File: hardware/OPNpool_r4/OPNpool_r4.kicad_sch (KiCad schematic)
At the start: 15 parts, among them J2 RS485-TERM-SPTAF, U1 MAX3485CSA+

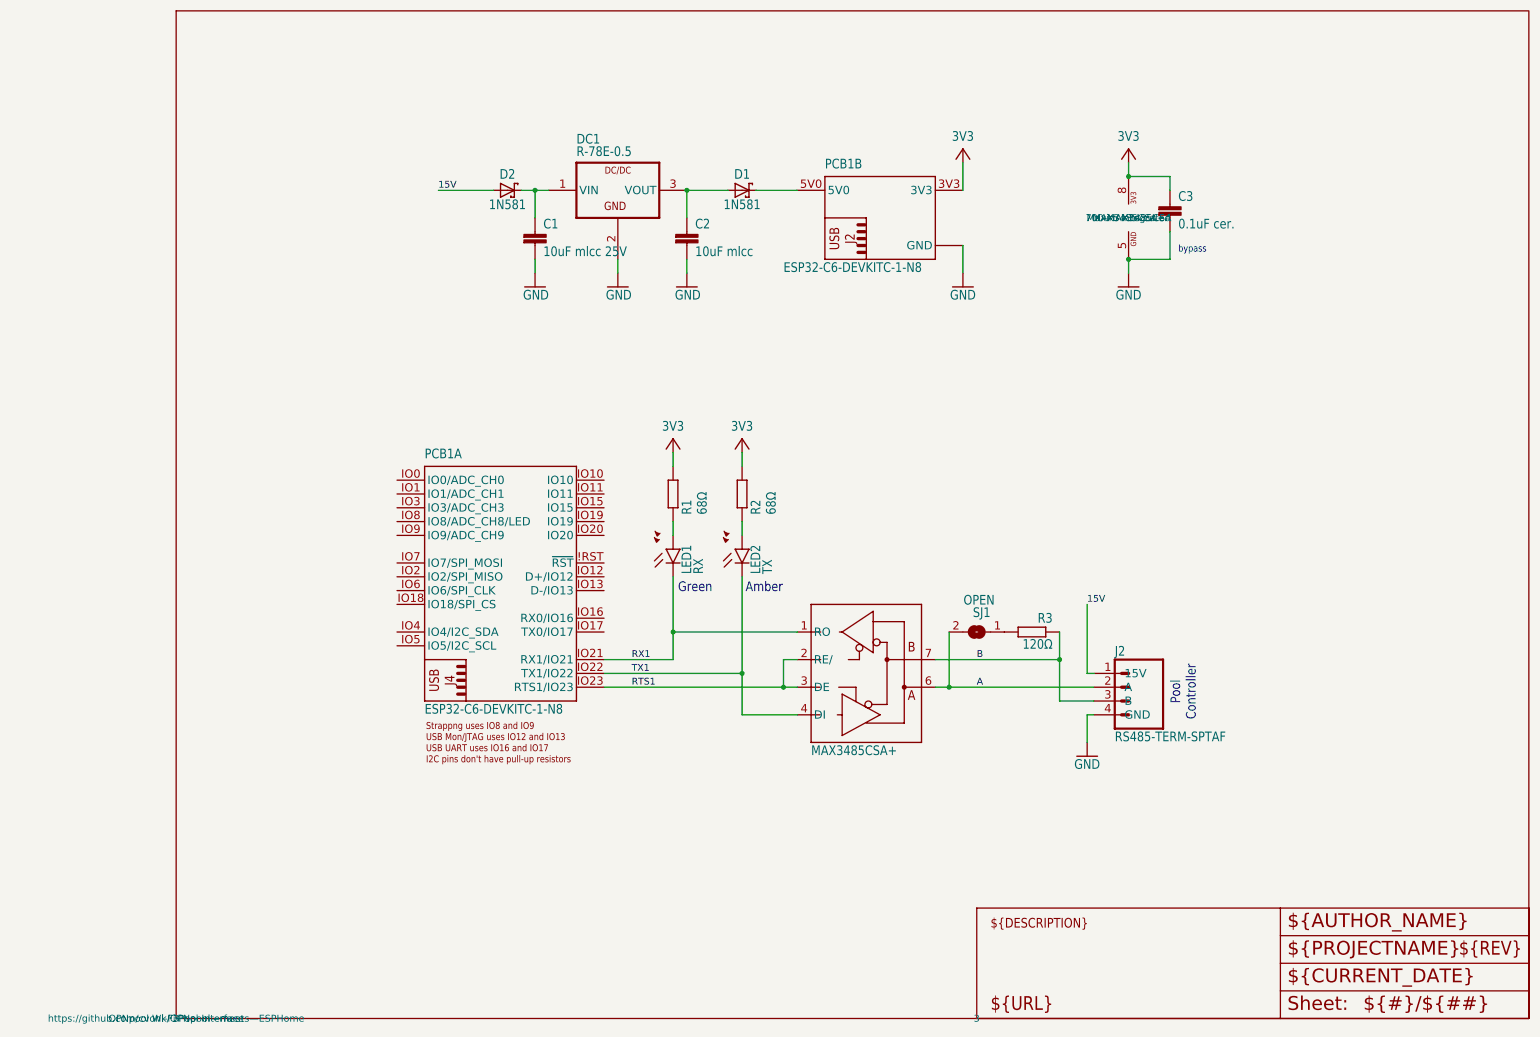
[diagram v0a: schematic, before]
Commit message: move from Eagle to KiCad symbols
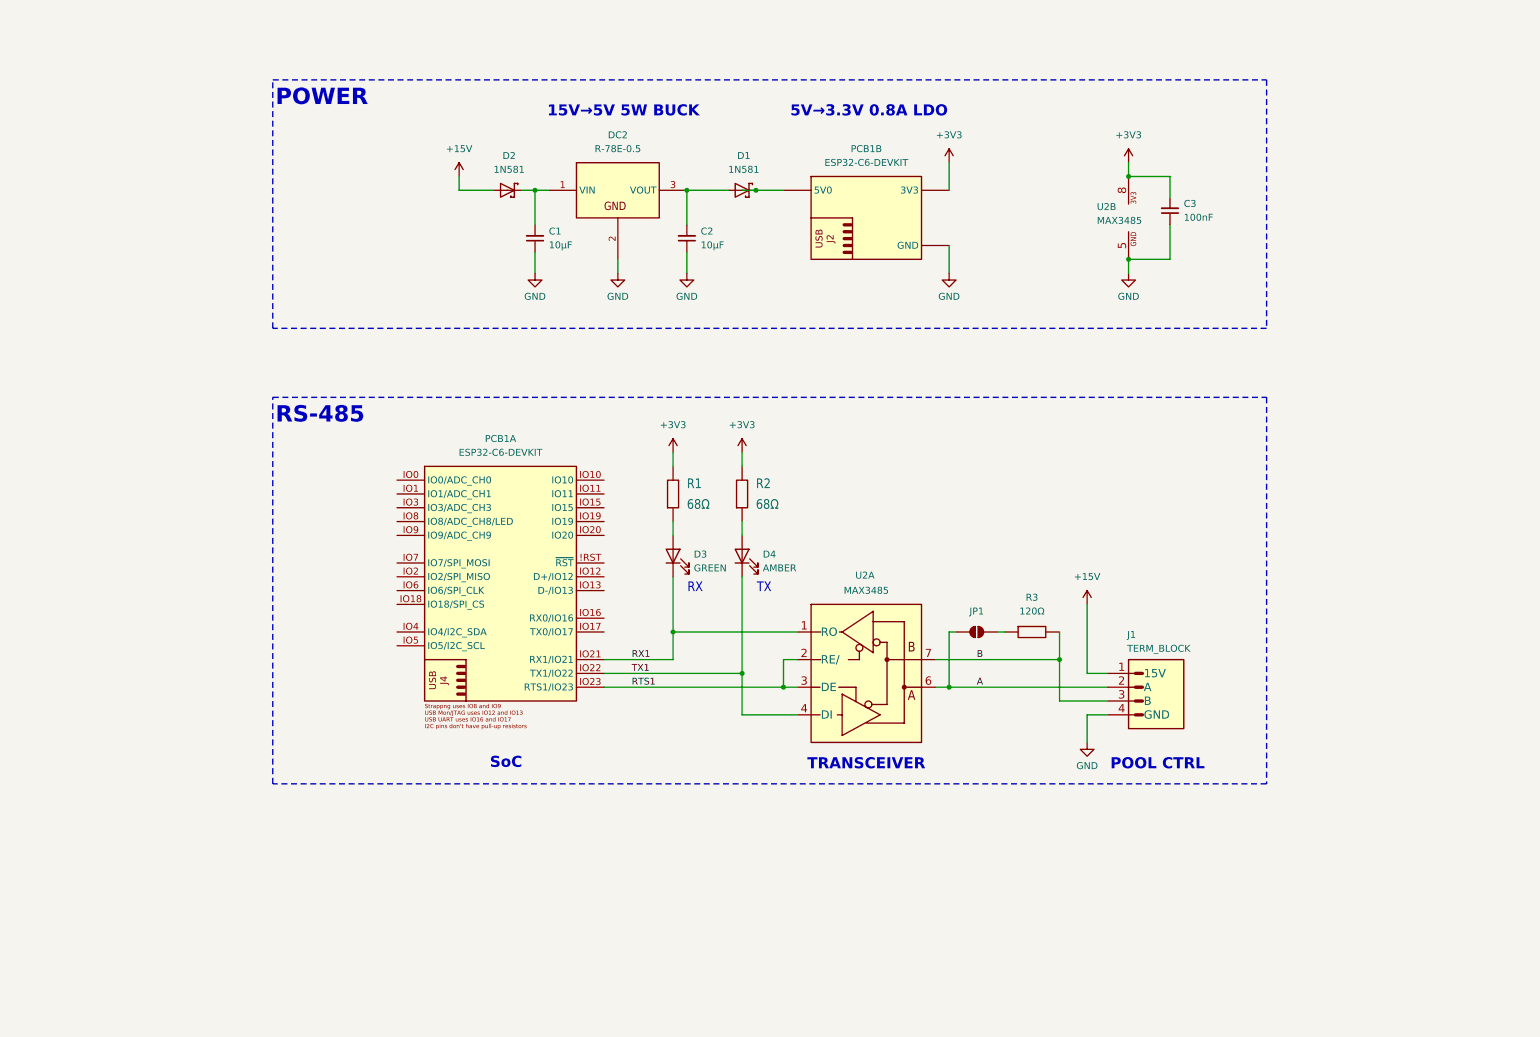
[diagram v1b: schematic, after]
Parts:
- removed C1: 10uF mlcc 25V, OPNpool r4:C0805K, symbol OPNpool r4-eagle-import:C-EUC0805K
- removed C2: 10uF mlcc, OPNpool r4:C0805K, symbol OPNpool r4-eagle-import:C-EUC0805K
- removed C3: 0.1uF cer., OPNpool r4:C0805K, symbol OPNpool r4-eagle-import:C-EUC0805K
- removed D1, D2: 1N581, OPNpool r4:DO41-7.6, symbol OPNpool r4-eagle-import:1N581
- removed DC1: R-78E-0.5, OPNpool r4:SIP3, symbol OPNpool r4-eagle-import:R-78E-0.5
- removed J2: RS485-TERM-SPTAF, OPNpool r4:SPTAF1_4-5,0-LL, symbol OPNpool r4-eagle-import:RS485-TERM-SPTAF
- removed LED1: RX, OPNpool r4:CHIPLED_0805, symbol OPNpool r4-eagle-import:LEDCHIPLED_0805
- removed LED2: TX, OPNpool r4:CHIPLED_0805, symbol OPNpool r4-eagle-import:LEDCHIPLED_0805
- removed PCB1: ESP32-C6-DEVKITC-1-N8, OPNpool r4:MODULE_ESP32-C6-DEVKITC-1-N8, symbol OPNpool r4-eagle-import:ESP32-C6-DEVKITC-1-N8
- removed R1, R2: 68Ω, OPNpool r4:R0805, symbol OPNpool r4-eagle-import:R-EU_R0805
- removed R3: 120Ω, OPNpool r4:R0805, symbol OPNpool r4-eagle-import:R-EU_R0805
- removed SJ1: OPEN, OPNpool r4:SJ, symbol OPNpool r4-eagle-import:SJ
- removed U1: MAX3485CSA+, OPNpool r4:SO08, symbol OPNpool r4-eagle-import:MAX3485CSA+
- added C1, C2: 10μF, Coert-Vonk:CAP CER 10µF 25V 0805, symbol Coert-Vonk:CAP CER 10µF 25V 0805
- added C3: 100nF, Coert-Vonk:CAP CER 100nF 25V 0805, symbol Coert-Vonk:CAP CER 100nF 25V 0805
- added D1, D2: 1N581, Coert-Vonk:DO41-DIO, symbol Coert-Vonk:DIODE SCHOTTKY 30V 1A 1N581 DO41
- added D3: GREEN, Coert-Vonk:LED-1206, symbol Coert-Vonk:LED GREEN CLEAR 1206
- added D4: AMBER, Coert-Vonk:LED-1206, symbol Coert-Vonk:LED AMBER CLEAR 1206
- added DC2: R-78E-0.5, Coert-Vonk:SIP3, symbol Coert-Vonk:REG 5V 3W BUCK R-78E-0.5
- added J1: TERM_BLOCK, Coert-Vonk:TERM BLOCK 4POS 45° 5mm PCB - CONN_1862437, symbol Coert-Vonk:TERM BLOCK 4POS 45° 5mm PCB
- added JP1: SolderJumper_2_Open, symbol Coert-Vonk:SolderJumper_2_Open
- added PCB1: ESP32-C6-DEVKIT, Coert-Vonk:EVAL ESP32-C6-DEVKITC, symbol Coert-Vonk:EVAL ESP32-C6-DEVKITC-1-N8
- added R1, R2: 68Ω, Coert-Vonk:REG 0805N_YAG, symbol Coert-Vonk:RES 68Ω ±1% 1/8W 0805
- added R3: 120Ω, Coert-Vonk:RES 120Ω 0805, symbol Coert-Vonk:RES 120Ω ±5% 1/4W 0805
- added U2: MAX3485, Coert-Vonk:SO08, symbol Coert-Vonk:IC MAX3485CSA+ TRANSCEIVER HALF SO08
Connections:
- net A: now also J1.2 (A), JP1.1 (A), U2.6 (A)
- net B: now also J1.3 (B), R3.2, U2.7 (B)
- net GND: now also C1.1, C2.1, C3.1, DC2.2 (GND), J1.4 (GND), PCB1.GND, PCB1.GND@1 (GND), PCB1.GND@2 (GND), PCB1.GND@3 (GND), U2.5 (GND)
- net RTS1: now also PCB1.IO23 (RTS1/IO23), U2.2 (RE/), U2.3 (DE)
- net RX1: now also D3.1 (K), PCB1.IO21 (RX1/IO21), U2.1 (RO)
- net TX1: now also D4.1 (K), PCB1.IO22 (TX1/IO22), U2.4 (DI)
- new net: C1.2, D2.C, DC2.1 (VIN)
- new net: D3.2 (A), R1.1
- new net: JP1.2 (B), R3.1
- new net: C2.2, D1.A, DC2.3 (VOUT)
- new net: D1.C, PCB1.5V0
- new net: D4.2 (A), R2.1
- new net +15V: D2.A, J1.1 (15V)
- new net +3V3: C3.2, PCB1.3V3, R1.2, R2.2, U2.8 (VCC)
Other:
- note added: "15V→5V 5W BUCK"
- note added: "5V→3.3V 0.8A LDO"
- note added: "POOL CTRL"
- note added: "POWER"
- note added: "RS-485"
- note added: "RX"
- note added: "SoC"
- note added: "TRANSCEIVER"
- note added: "TX"
- note removed: "Amber"
- note removed: "Green"
- note removed: "Pool Controller"
- note removed: "bypass"
- company: (none) -> https://github.com/cvonk/OPNpool
- title: (none) -> OPNpool

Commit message: Fix ERC errors
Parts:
- removed D1: 1N581, Coert-Vonk:DO41-DIO, symbol Coert-Vonk:DIODE SCHOTTKY 30V 1A 1N581 DO41
- removed DC2: R-78E-0.5, Coert-Vonk:SIP3, symbol Coert-Vonk:REG 5V 3W BUCK R-78E-0.5
- added D3: 1N581, Coert-Vonk:DO41-DIO, symbol Coert-Vonk:DIODE SCHOTTKY 30V 1A 1N581 DO41
- added DC1: R-78E-0.5, Coert-Vonk:SIP3, symbol Coert-Vonk:REG 5V 3W BUCK R-78E-0.5
- R1, R2: footprint Coert-Vonk:REG 0805N_YAG -> Coert-Vonk:RES 68Ω 0805
- renumbered D2 to D1, D3 to D2, U2 to U1
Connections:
- net GND: now also DC1.2 (GND)
- net at C1.2, D1.C: now also DC1.1 (VIN)
- net at C2.2: now also D3.A, DC1.3 (VOUT)
- net at PCB1.5V0: now also D3.C
- no-connect marks 0 -> 21
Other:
- note added: "15V→5V 5W Buck"
- note added: "Bus_term"
- note added: "POWER TRAIN"
- note added: "To pool controller"
- note added: "Transceiver"
- note removed: "15V→5V 5W BUCK"
- note removed: "POOL CTRL"
- note removed: "POWER"
- note removed: "TRANSCEIVER"
